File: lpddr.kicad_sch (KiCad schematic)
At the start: 34 parts, among them U12 MT53D512M32D2_WFBGA

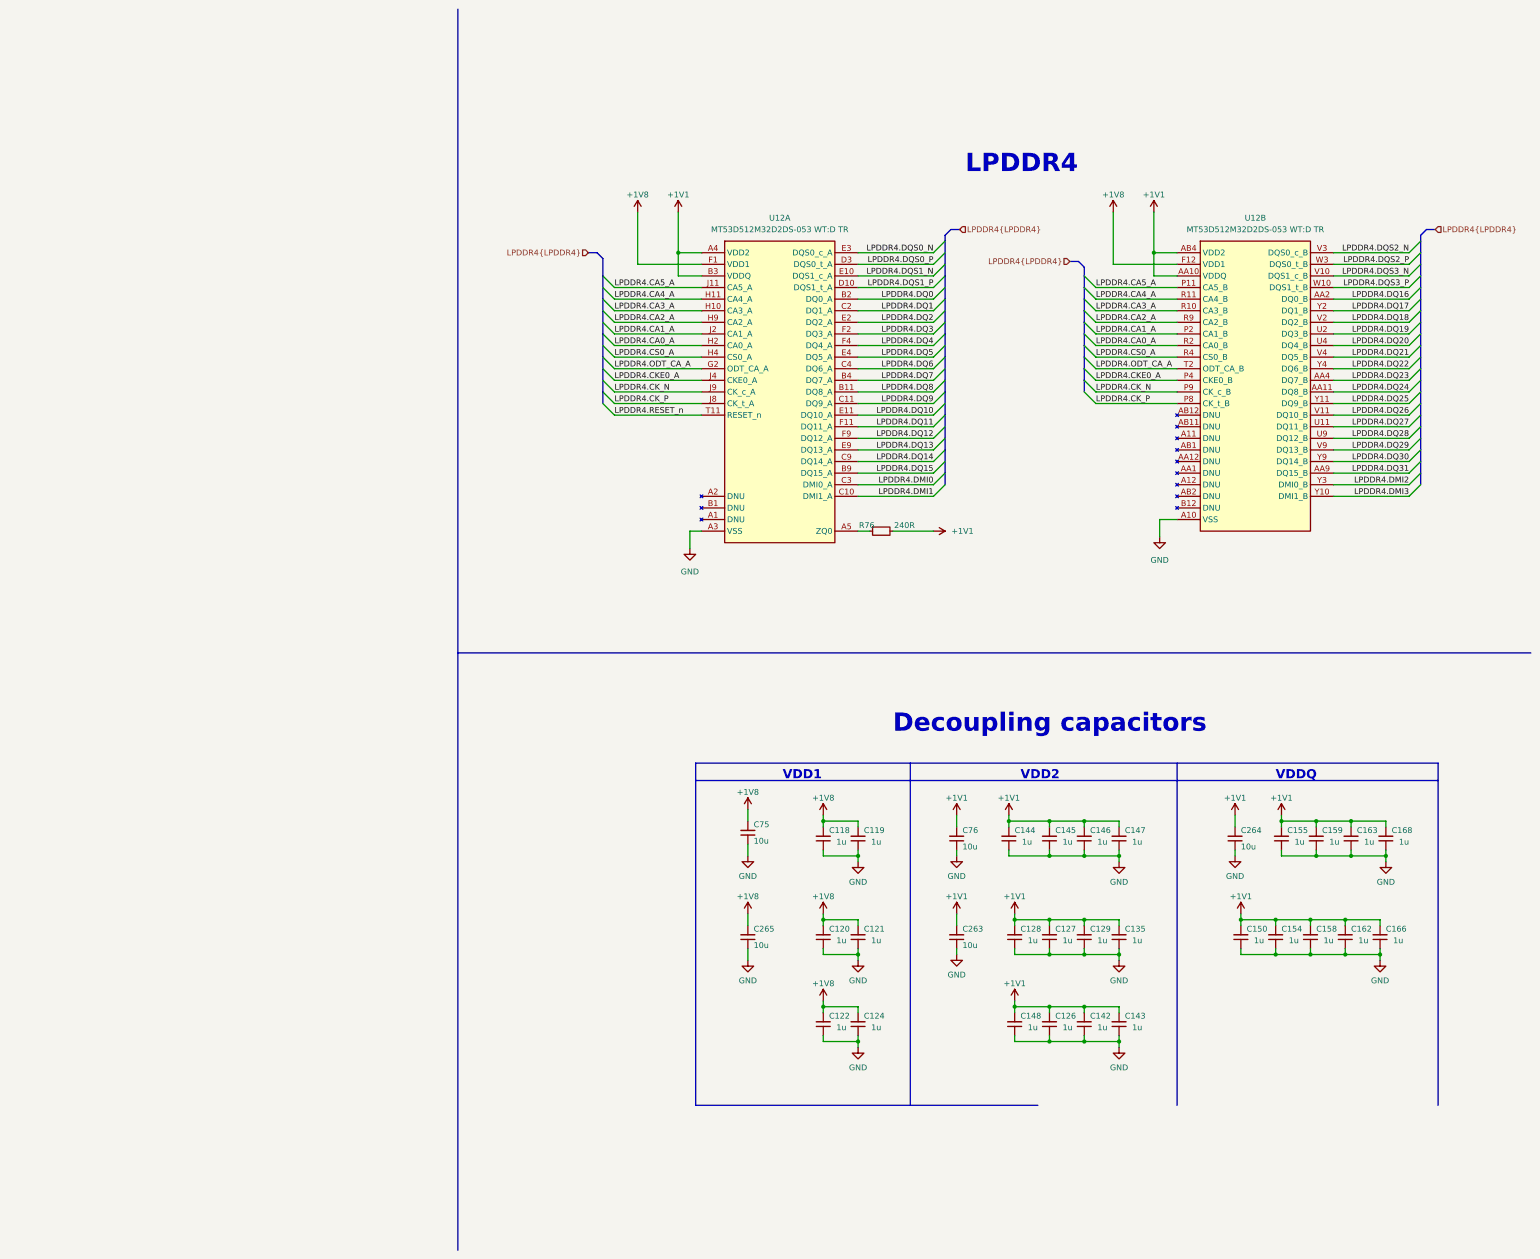
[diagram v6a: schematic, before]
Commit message: [#57505] Continue migration to hierarchical schematic
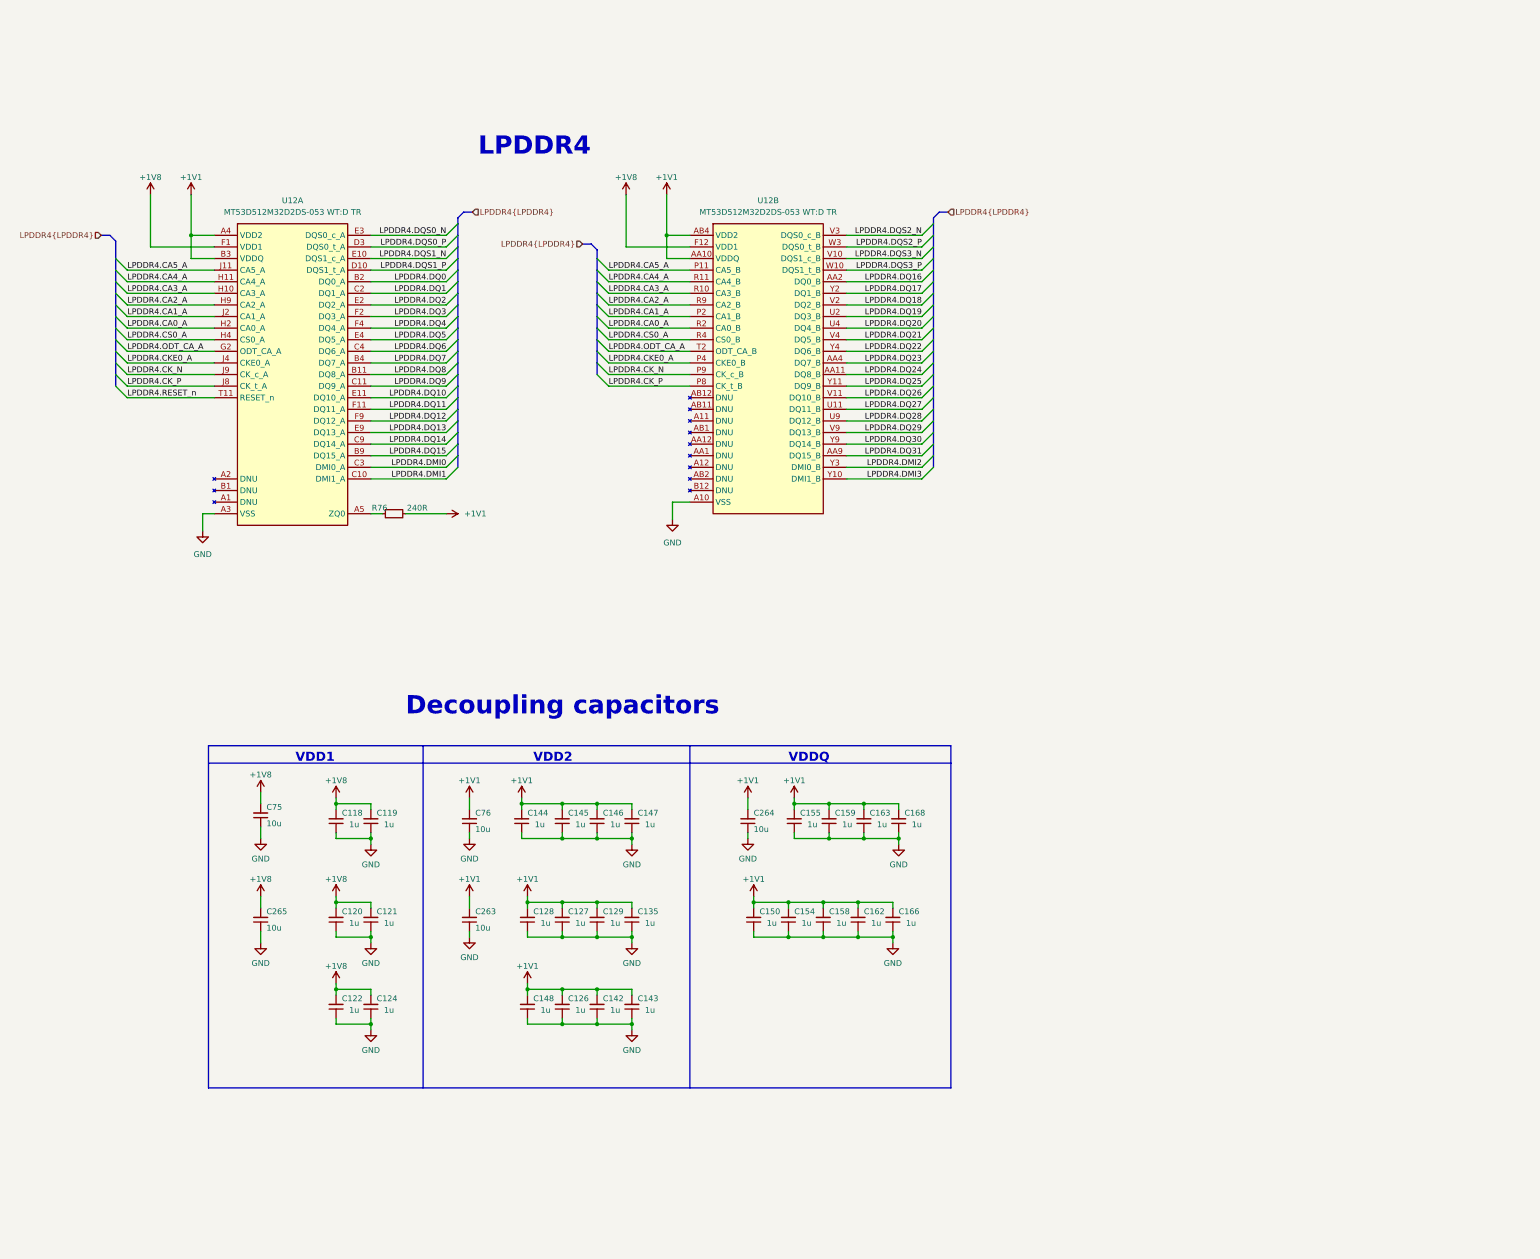
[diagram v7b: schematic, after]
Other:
- moved on the sheet: C118, C119, C120, C121, C122, C124, C126, C127, C128, C129, C135, C142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

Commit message: [#57422] Finishing touches
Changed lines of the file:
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@@
   (title_block
     (title "PolarFire SoM")
-    (date "2024-04-03")
+    (date "2024-04-08")
     (rev "1.0.0")
     (company "Antmicro Ltd")
@@
     (effects (font (size 2 2) (thickness 0.8) bold) (justify left bottom))
   )
-  (text "LPDDR4" (at 177.165 45.085 0)
+  (text "LPDDR4" (at 14.605 22.225 0)
     (effects (font (size 4 4) (thickness 0.8) bold) (justify left bottom))
   )
